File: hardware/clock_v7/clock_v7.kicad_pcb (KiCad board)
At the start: 2 copper layers, 119 x 92 mm, 151 parts, among them J1 RJ45, J10 KH-BNC50-3511, J11 KH-BNC50-3511, J12 Conn_01x06, J13 KH-BNC50-3511, J2 Conn_01x06_Pin, J3 KH-BNC50-3511, J4 Conn_01x04_Pin, J5 Conn_01x06_Pin, J6 Conn_01x04_Pin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

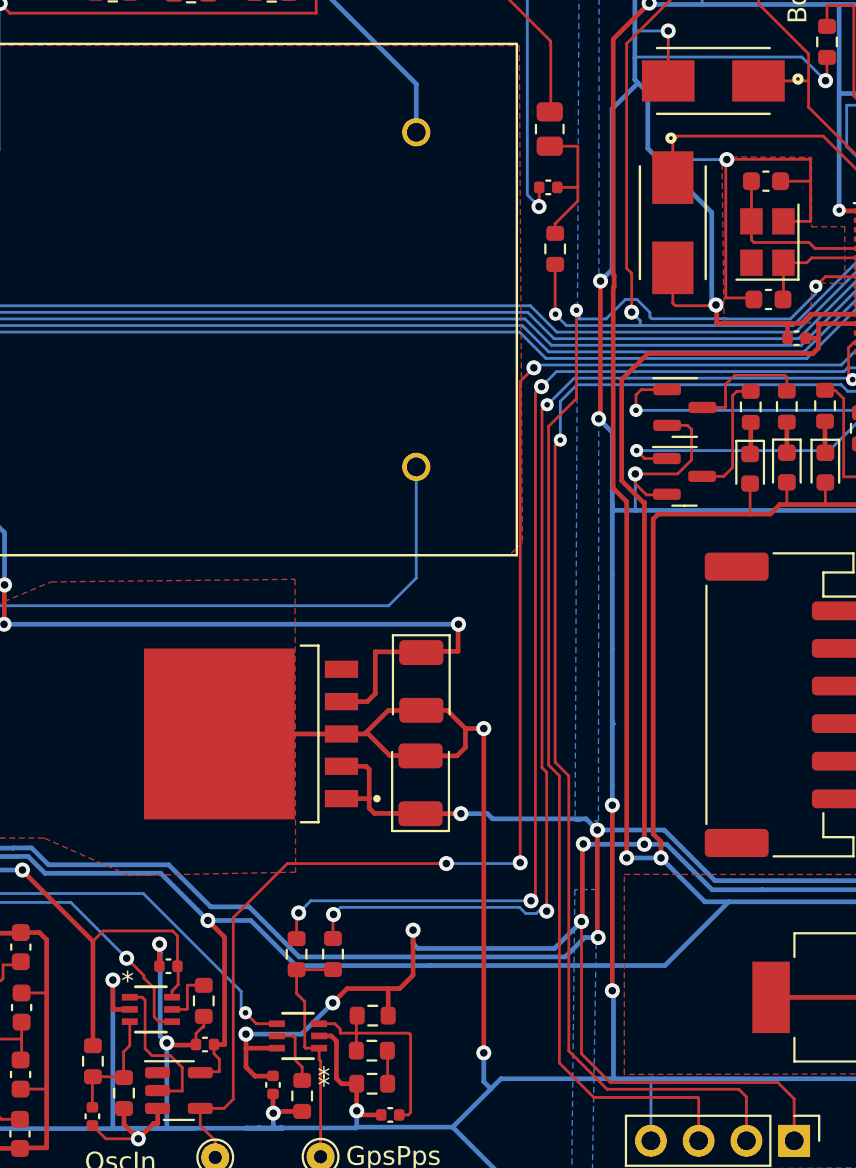
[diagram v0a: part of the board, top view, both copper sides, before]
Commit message: update comparator symbol on schematic
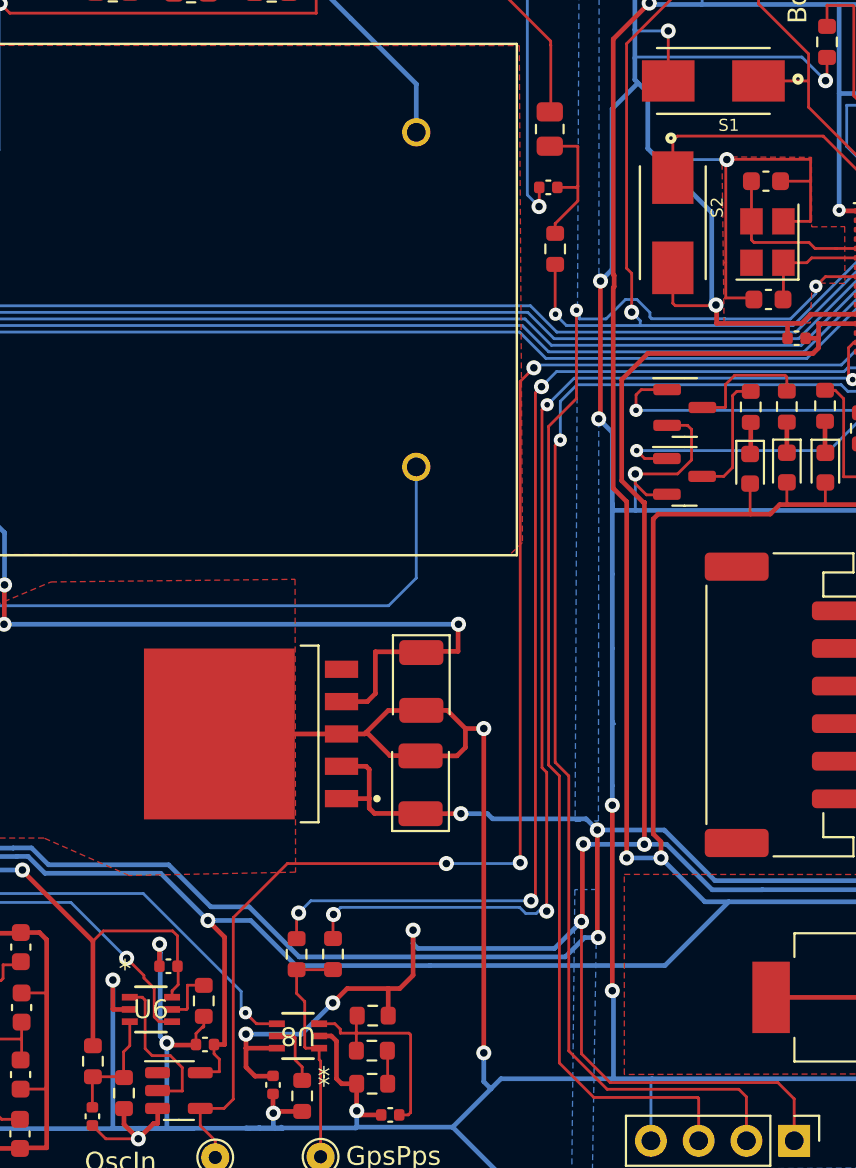
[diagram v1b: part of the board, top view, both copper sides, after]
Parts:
- L1, L2, L3, L4, L5, L6: value 1uF -> 1uH

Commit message: update opamp symbol on clock board
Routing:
- net Net-(U6-OUT): track 8.43 -> 7.90 mm
